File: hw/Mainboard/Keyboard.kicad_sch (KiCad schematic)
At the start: 9 parts, among them J18 KEYBOARD, J19 KEYBOARD_EX, U19 74LS145

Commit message: hw: touch ups (wip)
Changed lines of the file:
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@@
-    (stroke (width 0) (type default) (color 0 0 0 0))
-  )
-  (wire (pts (xy 226.06 146.05) (xy 217.17 146.05))
-    (stroke (width 0) (type default) (color 0 0 0 0))
-  )
-  (wire (pts (xy 204.47 138.43) (xy 217.17 138.43))
     (stroke (width 0) (type default) (color 0 0 0 0))
   )
@@
     (stroke (width 0) (type default) (color 0 0 0 0))
   )
+  (wire (pts (xy 227.33 133.35) (xy 227.33 130.81))
+    (stroke (width 0) (type default) (color 0 0 0 0))
+  )
   (bus (pts (xy 39.37 44.45) (xy 133.35 44.45))
     (stroke (width 0) (type default) (color 0 0 0 0))
@@
     (stroke (width 0) (type default) (color 0 0 0 0))
   )
-  (wire (pts (xy 204.47 135.89) (xy 226.06 135.89))
-    (stroke (width 0) (type default) (color 0 0 0 0))
-  )
   (wire (pts (xy 123.19 68.58) (xy 196.85 68.58))
     (stroke (width 0) (type default) (color 0 0 0 0))
@@
     (stroke (width 0) (type default) (color 0 0 0 0))
   )
+  (wire (pts (xy 227.33 142.24) (xy 228.6 142.24))
+    (stroke (width 0) (type default) (color 0 0 0 0))
+  )
   (wire (pts (xy 123.19 76.2) (xy 196.85 76.2))
     (stroke (width 0) (type default) (color 0 0 0 0))
@@
     (stroke (width 0) (type default) (color 0 0 0 0))
   )
+  (wire (pts (xy 227.33 138.43) (xy 227.33 142.24))
+    (stroke (width 0) (type default) (color 0 0 0 0))
+  )
   (wire (pts (xy 149.86 45.72) (xy 149.86 48.26))
     (stroke (width 0) (type default) (color 0 0 0 0))
   )
-  (wire (pts (xy 226.06 135.89) (xy 226.06 146.05))
+  (wire (pts (xy 227.33 130.81) (xy 228.6 130.81))
     (stroke (width 0) (type default) (color 0 0 0 0))
   )
@@
     (stroke (width 0) (type default) (color 0 0 0 0))
   )
-  (wire (pts (xy 217.17 138.43) (xy 217.17 139.7))
-    (stroke (width 0) (type default) (color 0 0 0 0))
-  )
   (wire (pts (xy 46.99 68.58) (xy 97.79 68.58))
     (stroke (width 0) (type default) (color 0 0 0 0))
@@
   )
   (wire (pts (xy 93.98 57.15) (xy 93.98 99.06))
-    (stroke (width 0) (type default) (color 0 0 0 0))
-  )
-  (wire (pts (xy 217.17 146.05) (xy 217.17 144.78))
     (stroke (width 0) (type default) (color 0 0 0 0))
   )
@@
   (label "R3" (at 196.85 76.2 180)
     (effects (font (size 1.27 1.27)) (justify right bottom))
+  )
+  (label "VSS" (at 228.6 142.24 0)
+    (effects (font (size 1.27 1.27)) (justify left bottom))
+  )
+  (label "VCC" (at 228.6 130.81 0)
+    (effects (font (size 1.27 1.27)) (justify left bottom))
   )
   (label "KEY_ROW2" (at 46.99 73.66 0)
@@
     (pin "1")
   )
-  (symbol (lib_id "Device:C_Small") (at 217.17 142.24 0) (mirror x) (unit 1)
+  (symbol (lib_id "Device:C_Small") (at 227.33 135.89 0) (mirror x) (unit 1)
     (in_bom yes) (on_board yes)
-    (property "Reference" "C98" (id 0) (at 219.5068 143.4084 0)
+    (property "Reference" "C98" (id 0) (at 229.6668 137.0584 0)
       (effects (font (size 1.27 1.27)) (justify left))
     )
-    (property "Value" "10u" (id 1) (at 219.5068 141.097 0)
+    (property "Value" "10u" (id 1) (at 229.6668 134.747 0)
       (effects (font (size 1.27 1.27)) (justify left))
     )
-    (property "Footprint" "Capacitor_SMD:C_0603_1608Metric" (id 2) (at 217.17 142.24 0)
-      (effects (font (size 1.27 1.27)) hide)
-    )
-    (property "Datasheet" "https://datasheet.lcsc.com/lcsc/2304140030_Samsung-Electro-Mechanics-CL10A106MA8NRNC_C96446.pdf" (id 3) (at 217.17 142.24 0)
-      (effects (font (size 1.27 1.27)) hide)
-    )
-    (property "LCSC" "C96446" (id 4) (at 217.17 142.24 0)
-      (effects (font (size 1.27 1.27)) hide)
-    )
+    (property "Footprint" "Capacitor_SMD:C_0603_1608Metric" (id 2) (at 227.33 135.89 0)
+      (effects (font (size 1.27 1.27)) hide)
+    )
+    (property "Datasheet" "https://datasheet.lcsc.com/lcsc/2304140030_Samsung-Electro-Mechanics-CL10A106MA8NRNC_C96446.pdf" (id 3) (at 227.33 135.89 0)
+      (effects (font (size 1.27 1.27)) hide)
+    )
+    (property "LCSC" "C96446" (id 4) (at 227.33 135.89 0)
+      (effects (font (size 1.27 1.27)) hide)
+    )

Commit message: hw: caps & logos (wip)
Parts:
- removed C98: 10u, Capacitor_SMD:C_0603_1608Metric, symbol Device:C_Small
- added C92: 1u, Capacitor_SMD:C_0402_1005Metric, symbol Device:C_Small
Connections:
- net +5V: now also C92.1
- net PD_GND: now also C92.2
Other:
- title: CBM PET Mainboard Replacement -> EconoPET 40/8096
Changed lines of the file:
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@@
   (paper "A")
   (title_block
-    (title "CBM PET Mainboard Replacement")
+    (title "EconoPET 40/8096")
+    (date "2023-10-01")
+    (rev "A")
   )
   (junction (at 157.48 34.29) (diameter 0) (color 0 0 0 0)
@@
     (stroke (width 0) (type default) (color 0 0 0 0))
   )
-  (wire (pts (xy 227.33 133.35) (xy 227.33 130.81))
-    (stroke (width 0) (type default) (color 0 0 0 0))
-  )
   (bus (pts (xy 39.37 44.45) (xy 133.35 44.45))
     (stroke (width 0) (type default) (color 0 0 0 0))
@@
     (stroke (width 0) (type default) (color 0 0 0 0))
   )
-  (wire (pts (xy 227.33 142.24) (xy 228.6 142.24))
-    (stroke (width 0) (type default) (color 0 0 0 0))
-  )
   (wire (pts (xy 123.19 76.2) (xy 196.85 76.2))
     (stroke (width 0) (type default) (color 0 0 0 0))
@@
     (stroke (width 0) (type default) (color 0 0 0 0))
   )
-  (wire (pts (xy 227.33 138.43) (xy 227.33 142.24))
-    (stroke (width 0) (type default) (color 0 0 0 0))
-  )
   (wire (pts (xy 149.86 45.72) (xy 149.86 48.26))
-    (stroke (width 0) (type default) (color 0 0 0 0))
-  )
-  (wire (pts (xy 227.33 130.81) (xy 228.6 130.81))
     (stroke (width 0) (type default) (color 0 0 0 0))
   )
@@
   (label "R3" (at 196.85 76.2 180)
     (effects (font (size 1.27 1.27)) (justify right bottom))
-  )
-  (label "VSS" (at 228.6 142.24 0)
-    (effects (font (size 1.27 1.27)) (justify left bottom))
-  )
-  (label "VCC" (at 228.6 130.81 0)
-    (effects (font (size 1.27 1.27)) (justify left bottom))
   )
   (label "KEY_ROW2" (at 46.99 73.66 0)
@@
     (pin "2")
   )
+  (symbol (lib_id "Device:C_Small") (at 229.87 133.35 0) (unit 1)
+    (in_bom yes) (on_board yes)
+    (property "Reference" "C92" (id 0) (at 232.2068 132.1816 0)
+      (effects (font (size 1.27 1.27)) (justify left))
+    )
+    (property "Value" "1u" (id 1) (at 232.2068 134.493 0)
+      (effects (font (size 1.27 1.27)) (justify left))
+    )
+    (property "Footprint" "Capacitor_SMD:C_0402_1005Metric" (id 2) (at 229.87 133.35 0)
+      (effects (font (size 1.27 1.27)) hide)
+    )
+    (property "Datasheet" "https://datasheet.lcsc.com/lcsc/2304140030_Samsung-Electro-Mechanics-CL05A105KA5NQNC_C52923.pdf" (id 3) (at 229.87 133.35 0)
+      (effects (font (size 1.27 1.27)) hide)
+    )
+    (property "LCSC" "C52923" (id 4) (at 229.87 133.35 0)
+      (effects (font (size 1.27 1.27)) hide)
+    )
+    (pin "1")
+    (pin "2")
+  )
   (symbol (lib_id "PET:PowerTie_2") (at 110.49 31.75 270) (unit 1)
     (in_bom yes) (on_board yes) (fields_autoplaced)
@@
     (pin "9")
   )
+  (symbol (lib_id "power:+5V") (at 229.87 130.81 0) (unit 1)
+    (in_bom yes) (on_board yes) (fields_autoplaced)
+    (property "Reference" "#PWR0183" (id 0) (at 229.87 134.62 0)
+      (effects (font (size 1.27 1.27)) hide)
+    )
+    (property "Value" "+5V" (id 1) (at 229.87 125.73 0))
+    (property "Footprint" "" (id 2) (at 229.87 130.81 0)
+      (effects (font (size 1.27 1.27)) hide)
+    )
+    (property "Datasheet" "" (id 3) (at 229.87 130.81 0)
+      (effects (font (size 1.27 1.27)) hide)
+    )
+    (pin "1")
+  )
   (symbol (lib_id "PET:PD_GND") (at 194.31 97.79 0) (unit 1)
     (in_bom yes) (on_board yes) (fields_autoplaced)
@@
     (pin "1")
   )
-  (symbol (lib_id "Device:C_Small") (at 227.33 135.89 0) (mirror x) (unit 1)
-    (in_bom yes) (on_board yes)
-    (property "Reference" "C98" (id 0) (at 229.6668 137.0584 0)
-      (effects (font (size 1.27 1.27)) (justify left))
-    )
-    (property "Value" "10u" (id 1) (at 229.6668 134.747 0)
-      (effects (font (size 1.27 1.27)) (justify left))
-    )
-    (property "Footprint" "Capacitor_SMD:C_0603_1608Metric" (id 2) (at 227.33 135.89 0)
-      (effects (font (size 1.27 1.27)) hide)
-    )
-    (property "Datasheet" "https://datasheet.lcsc.com/lcsc/2304140030_Samsung-Electro-Mechanics-CL10A106MA8NRNC_C96446.pdf" (id 3) (at 227.33 135.89 0)
-      (effects (font (size 1.27 1.27)) hide)
-    )
-    (property "LCSC" "C96446" (id 4) (at 227.33 135.89 0)
-      (effects (font (size 1.27 1.27)) hide)
-    )
-    (pin "1")
-    (pin "2")
-  )
   (symbol (lib_id "power:+5V") (at 110.49 29.21 0) (unit 1)
     (in_bom yes) (on_board yes) (fields_autoplaced)
@@
     (pin "2")
   )
+  (symbol (lib_id "PET:PD_GND") (at 229.87 135.89 0) (unit 1)
+    (in_bom yes) (on_board yes) (fields_autoplaced)
+    (property "Reference" "#PWR0184" (id 0) (at 229.87 142.24 0)
+      (effects (font (size 1.27 1.27)) hide)
+    )
+    (property "Value" "PD_GND" (id 1) (at 229.87 140.97 0))
+    (property "Footprint" "" (id 2) (at 229.87 135.89 0)
+      (effects (font (size 1.27 1.27)) hide)
+    )
+    (property "Datasheet" "" (id 3) (at 229.87 135.89 0)
+      (effects (font (size 1.27 1.27)) hide)
+    )
+    (pin "1")
+  )
   (symbol (lib_id "Device:R_Pack04") (at 154.94 40.64 0) (unit 1)

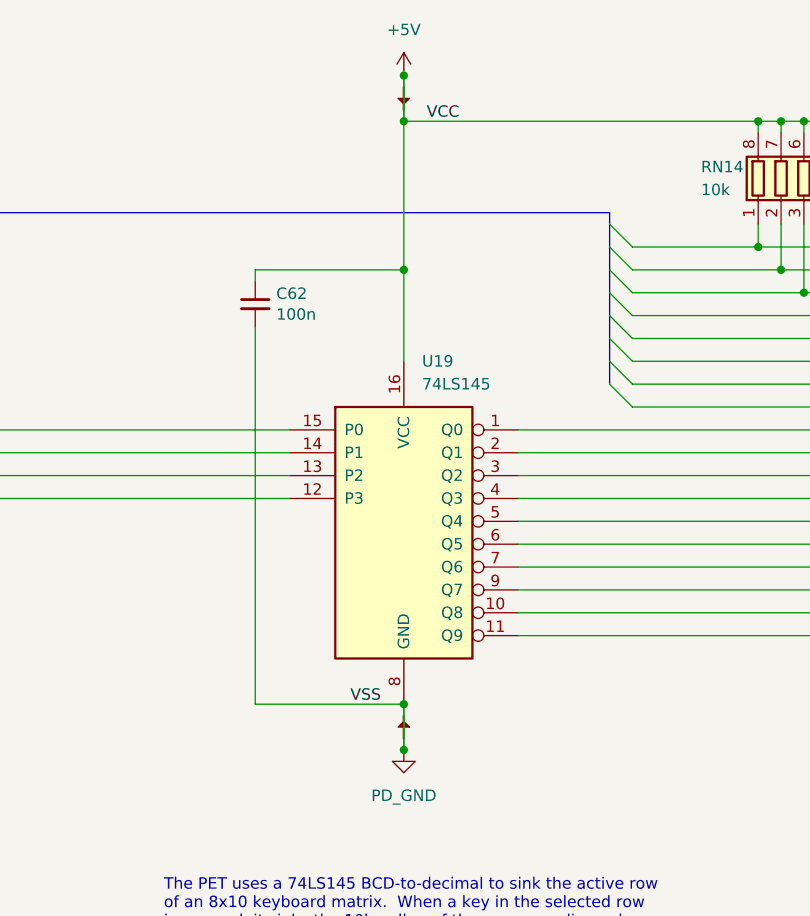
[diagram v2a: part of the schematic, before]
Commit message: hw: remove net/power ties
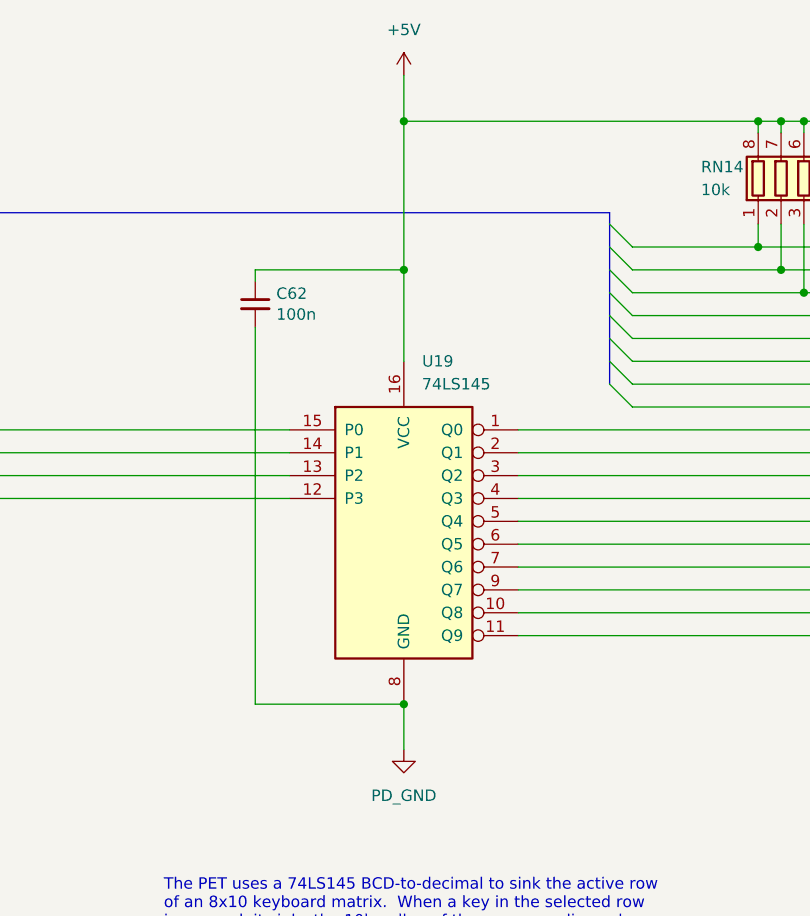
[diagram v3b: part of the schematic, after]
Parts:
- removed PT42, PT43: PowerTie_2, PET:NetTie-2_SMD_Pad_1.6_to_0.4mm, symbol PET:PowerTie_2
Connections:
- net +5V: no longer J19.5 (Pin_5)
- net PD_GND: no longer J19.7 (Pin_7)
- new net VCC: J19.5 (Pin_5)
- new net VSS: J19.7 (Pin_7)
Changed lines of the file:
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@@
   (junction (at 110.49 50.8) (diameter 0) (color 0 0 0 0)
   )
-  (junction (at 110.49 29.21) (diameter 0) (color 0 0 0 0)
-  )
   (junction (at 167.64 34.29) (diameter 0) (color 0 0 0 0)
   )
@@
   )
   (junction (at 154.94 34.29) (diameter 0) (color 0 0 0 0)
-  )
-  (junction (at 110.49 104.14) (diameter 0) (color 0 0 0 0)
   )
   (junction (at 175.26 66.04) (diameter 0) (color 0 0 0 0)
@@
     (effects (font (size 1.27 1.27)) (justify right bottom))
   )
-  (label "VCC" (at 113.03 34.29 0)
-    (effects (font (size 1.27 1.27)) (justify left bottom))
-  )
   (label "R0" (at 196.85 68.58 180)
-    (effects (font (size 1.27 1.27)) (justify right bottom))
-  )
-  (label "VSS" (at 107.95 99.06 180)
     (effects (font (size 1.27 1.27)) (justify right bottom))
   )
@@
     (pin "2")
   )
-  (symbol (lib_id "PET:PowerTie_2") (at 110.49 31.75 270) (unit 1)
-    (in_bom yes) (on_board yes) (fields_autoplaced)
-    (property "Reference" "PT42" (id 0) (at 112.395 31.75 0)
-      (effects (font (size 1.27 1.27)) hide)
-    )
-    (property "Value" "PowerTie_2" (id 1) (at 108.585 31.75 0)
-      (effects (font (size 1.27 1.27)) hide)
-    )
-    (property "Footprint" "PET:NetTie-2_SMD_Pad_1.6_to_0.4mm" (id 2) (at 110.49 31.75 0)
-      (effects (font (size 1.27 1.27)) hide)
-    )
-    (property "Datasheet" "~" (id 3) (at 110.49 31.75 0)
-      (effects (font (size 1.27 1.27)) hide)
-    )
-    (pin "1")
-    (pin "2")
-  )
   (symbol (lib_id "PET:PD_GND") (at 110.49 104.14 0) (unit 1)
     (in_bom yes) (on_board yes) (fields_autoplaced)
@@
     (pin "1")
   )
-  (symbol (lib_id "PET:PowerTie_2") (at 110.49 101.6 270) (mirror x) (unit 1)
-    (in_bom yes) (on_board yes) (fields_autoplaced)
-    (property "Reference" "PT43" (id 0) (at 112.395 101.6 0)
-      (effects (font (size 1.27 1.27)) hide)
-    )
-    (property "Value" "PowerTie_2" (id 1) (at 108.585 101.6 0)
-      (effects (font (size 1.27 1.27)) hide)
-    )
-    (property "Footprint" "PET:NetTie-2_SMD_Pad_1.6_to_0.4mm" (id 2) (at 110.49 101.6 0)
-      (effects (font (size 1.27 1.27)) hide)
-    )
-    (property "Datasheet" "~" (id 3) (at 110.49 101.6 0)
-      (effects (font (size 1.27 1.27)) hide)
-    )
-    (pin "1")
-    (pin "2")
-  )
   (symbol (lib_id "PET:PD_GND") (at 229.87 135.89 0) (unit 1)
